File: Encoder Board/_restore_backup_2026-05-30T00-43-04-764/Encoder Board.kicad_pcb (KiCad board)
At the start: 2 copper layers, 51.8 x 57 mm, 20 parts, among them J1 Conn_02x05_Odd_Even, J2 Conn_02x05_Odd_Even, J3 Conn_01x02_Pin, J4 Conn_01x02_Pin, J5 Conn_01x20, J6 Conn_01x20, J7 Conn_02x04_Odd_Even, U1 AM26LV32xD

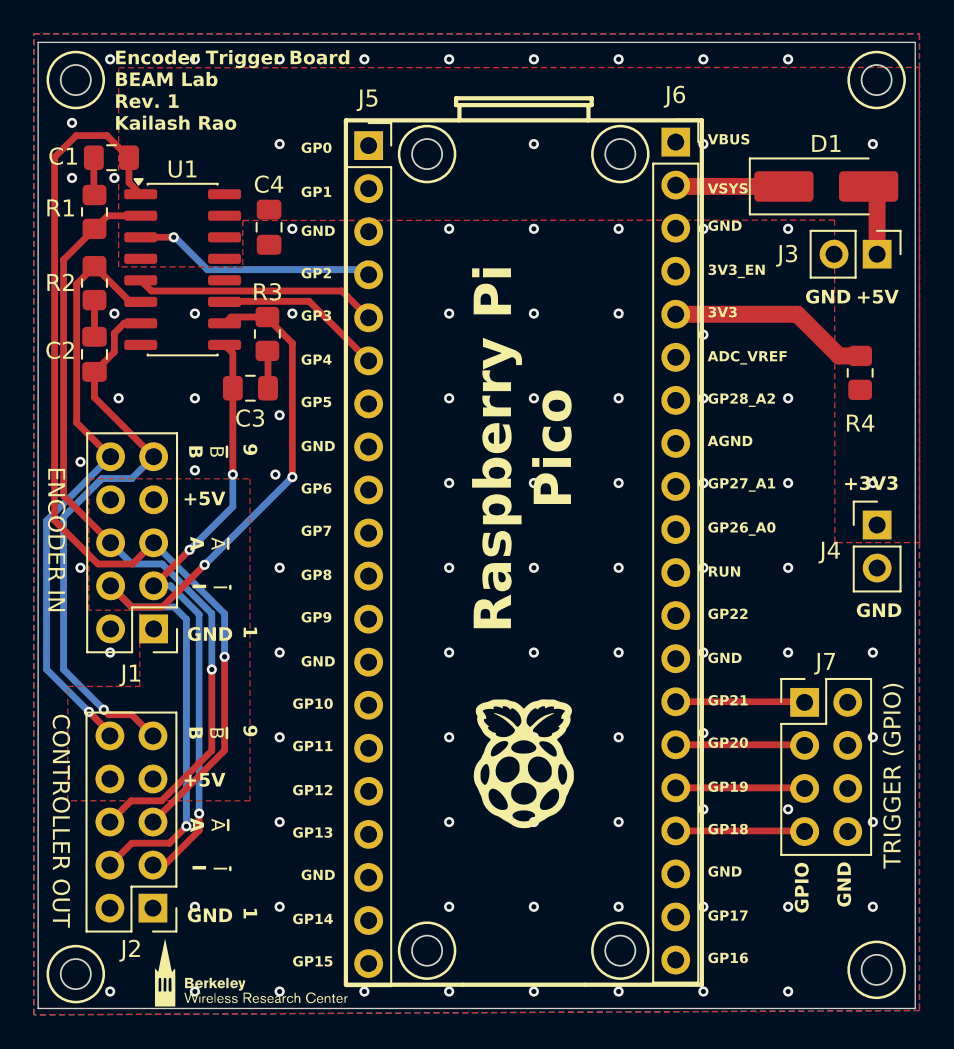
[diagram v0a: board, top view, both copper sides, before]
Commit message: add BWRC logo, generate new gerbers
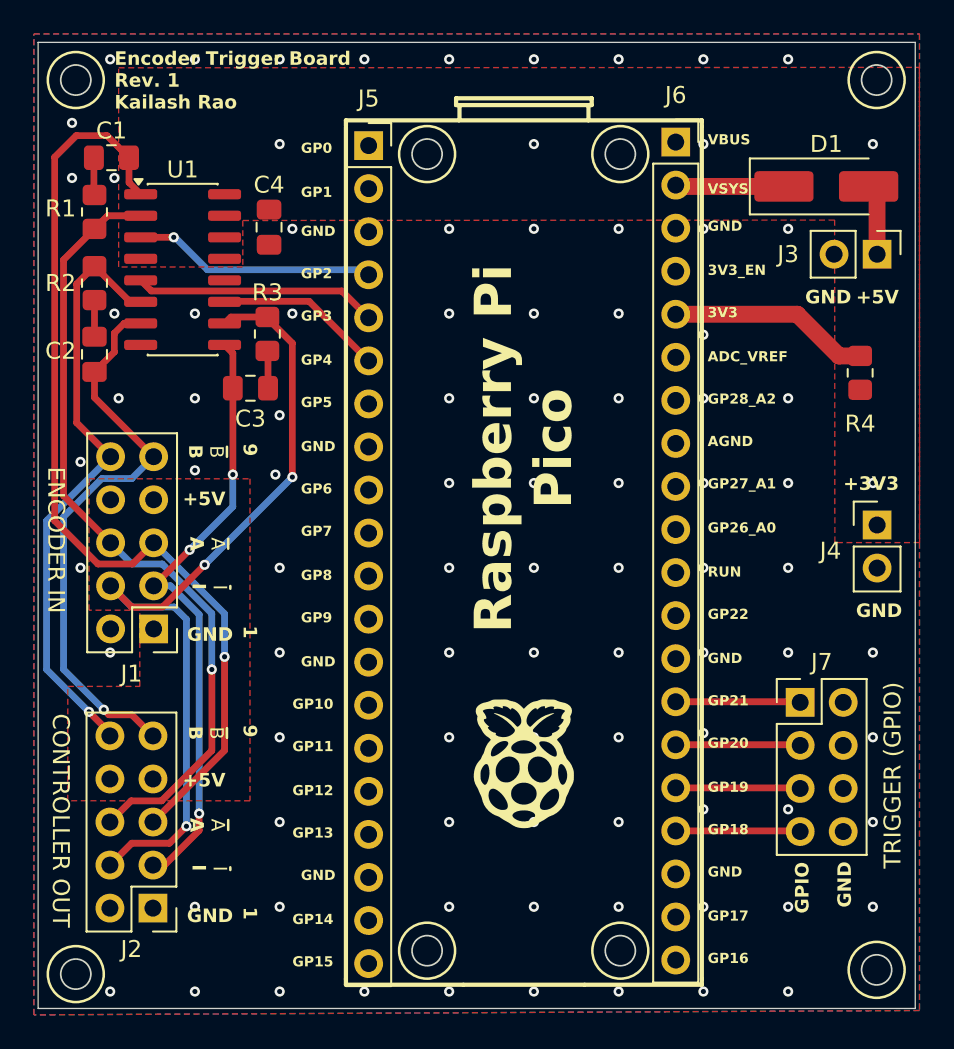
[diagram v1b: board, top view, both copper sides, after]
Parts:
- removed the G*** at (77.5, 82.0)
- J7: value Conn_02x04_Odd_Even -> Conn_02x04_Counter_Clockwise
- moved J7 0.27 mm to (110.0, 66.2)
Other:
- board text added: "Encoder Trigger Board Rev. 1 Kailash Rao"
- board text removed: "Encoder Trigger Board BEAM Lab Rev. 1 Kailash Rao"
